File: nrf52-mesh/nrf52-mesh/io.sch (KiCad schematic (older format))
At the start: 22 parts

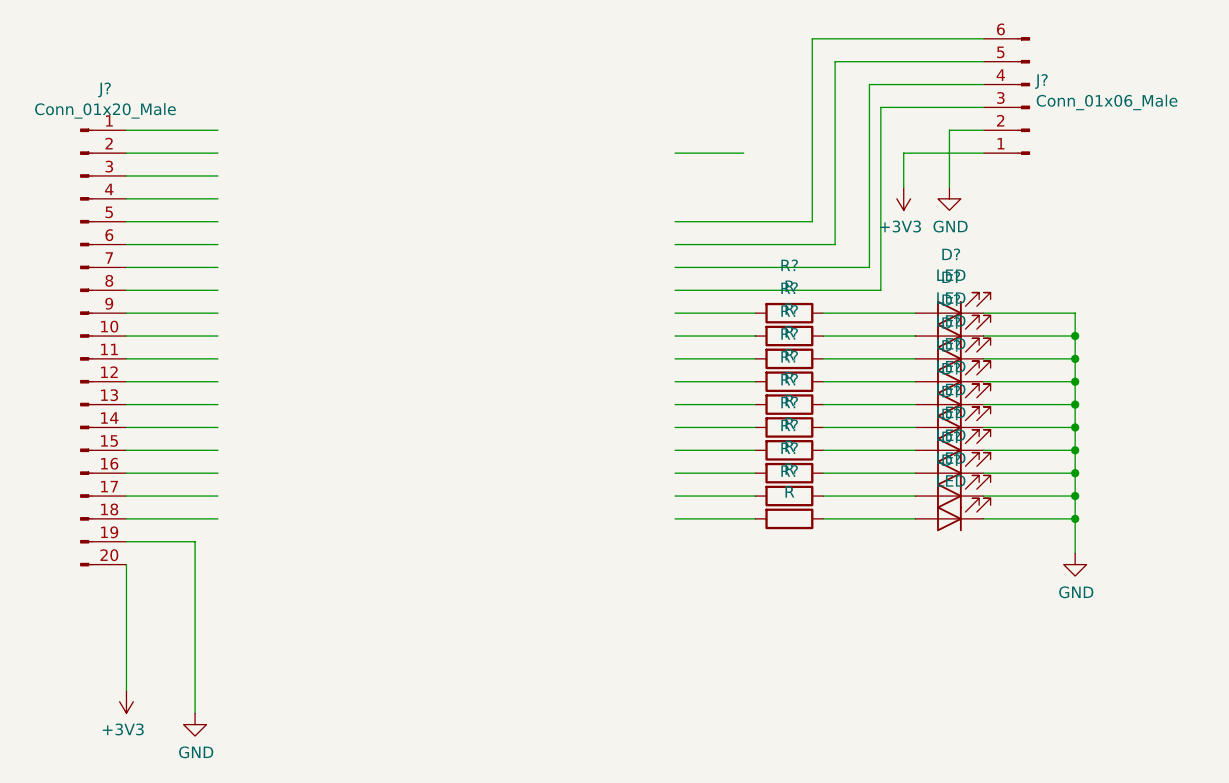
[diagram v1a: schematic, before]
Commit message: CP2102N + MAX1555 + FAN5341 + TPS560200 + TLV62568
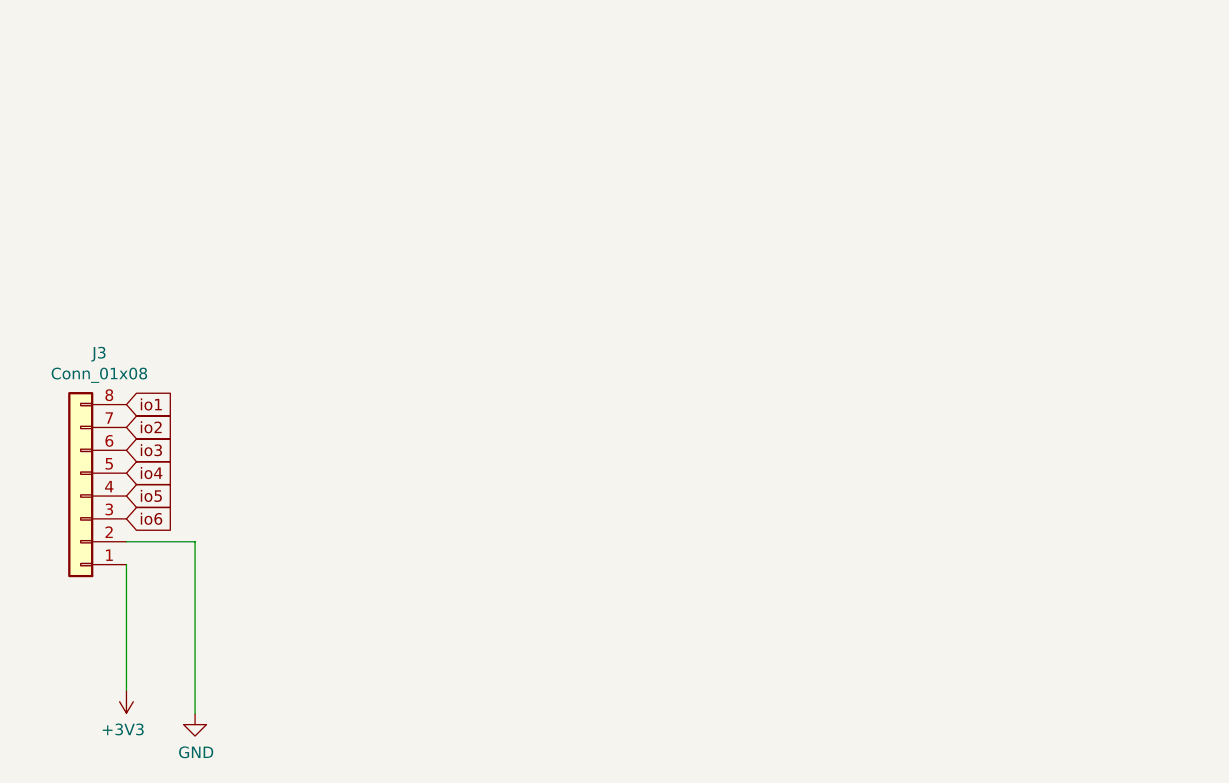
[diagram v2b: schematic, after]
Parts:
- removed D? (x10): LED, LED_SMD:LED_1206_3216Metric, symbol Device:LED
- removed J?: Conn_01x20_Male, Connector_PinHeader_2.54mm:PinHeader_1x20_P2.54mm_Vertical, symbol Connector:Conn_01x20_Male
- removed J?: Conn_01x06_Male, Connector_PinHeader_2.54mm:PinHeader_1x06_P2.54mm_Vertical, symbol Connector:Conn_01x06_Male
- removed R? (x4): R, Resistor_SMD:R_0402_1005Metric, symbol Device:R
- removed R? (x4): R, Resistor_SMD:R_0805_2012Metric, symbol Device:R
- removed R? (x2): R, Resistor_SMD:R_1206_3216Metric, symbol Device:R
- added J3: Conn_01x08, Connector_PinSocket_2.54mm:PinSocket_1x08_P2.54mm_Vertical, symbol Connector_Generic:Conn_01x08
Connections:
- net labels added: io1, io2, io3, io4, io5, io6
- wire segments 78 -> 3
